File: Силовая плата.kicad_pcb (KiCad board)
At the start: 6 copper layers, 67 x 90.2 mm, 71 parts, among them J1 A, J2 B, J3 C, J4 IN-, J5 IN+, J6 Conn_02x10_Odd_Even, Q1 2N7002, Q2 2N7002, Q3 2N7002, Q4 2N7002, Q5 2N7002, Q6 2N7002, Q7 BSS214NW

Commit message: Отчётная версия
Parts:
- removed H3, H4: MountingHole, MountingHole:MountingHole_3.2mm_M3
- added J2: A, Connector_My:Power_Wire, F.Cu at (167.1, 124.9)
- added J8: A, Connector_My:Power_Wire, F.Cu at (132.2, 124.9)
- moved C1 70.7 mm to (157.0, 100.8)
- moved C10 70.7 mm to (145.6, 106.5)
- moved C12 70.7 mm to (134.1, 106.5)
- moved C14 70.7 mm to (145.6, 100.8)
- moved C16 70.7 mm to (141.7, 100.8)
- moved C17 70.7 mm to (137.9, 106.5)
- moved C18 70.7 mm to (145.6, 106.5)
- moved C19 70.7 mm to (157.0, 111.9)
- moved C2 70.7 mm to (141.7, 95.1)
- moved C21 70.7 mm to (153.2, 95.1)
- moved C22 70.7 mm to (137.9, 95.1)
- moved C24 70.7 mm to (137.9, 106.5)
- moved C25 70.7 mm to (141.7, 111.9)
- moved C26 70.7 mm to (145.6, 111.9)
- moved C27 70.7 mm to (137.9, 111.8)
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- renumbered C33 to C1, C47 to C10, C1 to C11, C6 to C12, C9 to C13, C12 to C14, C18 to C16, C21 to C17, C24 to C18, C27 to C19, C35 to C2, C40 to C20, C34 to C21, C36 to C22, C2 to C23, C7 to C24, C10 to C25, C13 to C26, C16 to C27, C19 to C28, C22 to C29, C37 to C3, C25 to C30, C28 to C31, C31 to C32, C3 to C33, C8 to C34, C11 to C35, C17 to C36, C20 to C37, C23 to C38, C26 to C39, C39 to C4, C29 to C40, C32 to C41, C38 to C43, C4 to C44, C5 to C45, C14 to C46, C30 to C47, C41 to C5, C43 to C6, C44 to C7, C45 to C8, C46 to C9, J2 to J3, J3 to J4, J4 to J5, J5 to J6, J6 to J7, Q3 to Q2, Q5 to Q3, Q2 to Q4, Q4 to Q5, R3 to R2
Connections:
- net SCL renamed SCL_MCU
- net SDA renamed SDA_MCU
- net ~{OS} renamed ~{OS}_MCU
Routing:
- net B: track 3.23 -> 12.1 mm
- net G4: track 17.6 -> 21.6 mm
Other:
- board size 67 x 90.2 mm -> 67 x 90.5 mm

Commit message: Изменил разъём 2.54мм на 2.0мм
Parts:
- J7: footprint Connector_PinSocket_2.54mm:PinSocket_2x10_P2.54mm_Vertical -> Connector_PinSocket_2.00mm:PinSocket_2x10_P2.00mm_Vertical
- moved J7 2.32 mm to (150.4, 70.7)
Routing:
- net ~{OS}_MCU: track 78.1 -> 81.5 mm
- net Shunt_1: track 14.1 -> 16.6 mm
- net G3: track 12.8 -> 14.6 mm
- net B: track 12.1 -> 13.4 mm
- net SDA_MCU: track 81.9 -> 83.0 mm
- net SCL_MCU: track 77.7 -> 78.8 mm
- net G4: track 21.6 -> 22.4 mm
- net G2: track 20.3 -> 21.1 mm
- net C: track 8.78 -> 9.44 mm

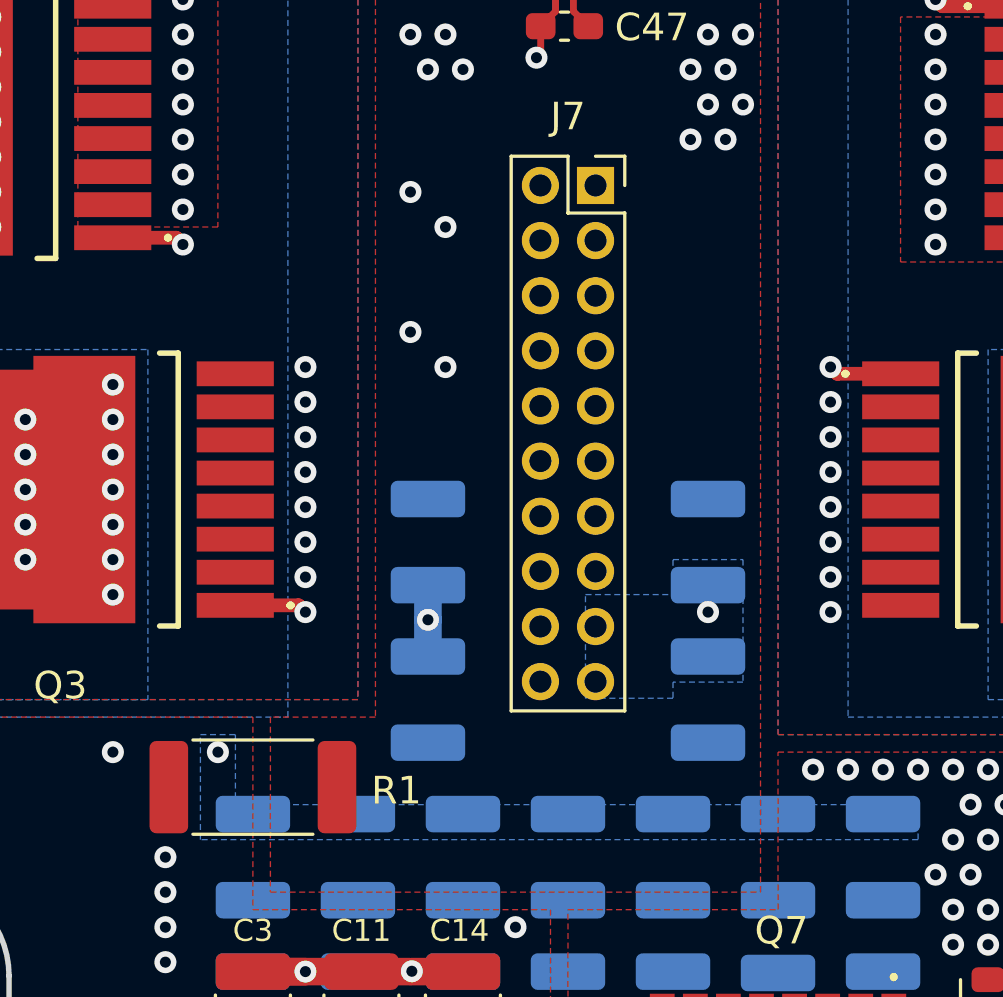
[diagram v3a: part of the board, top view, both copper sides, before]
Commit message: Убрал слабое место полигона +24В
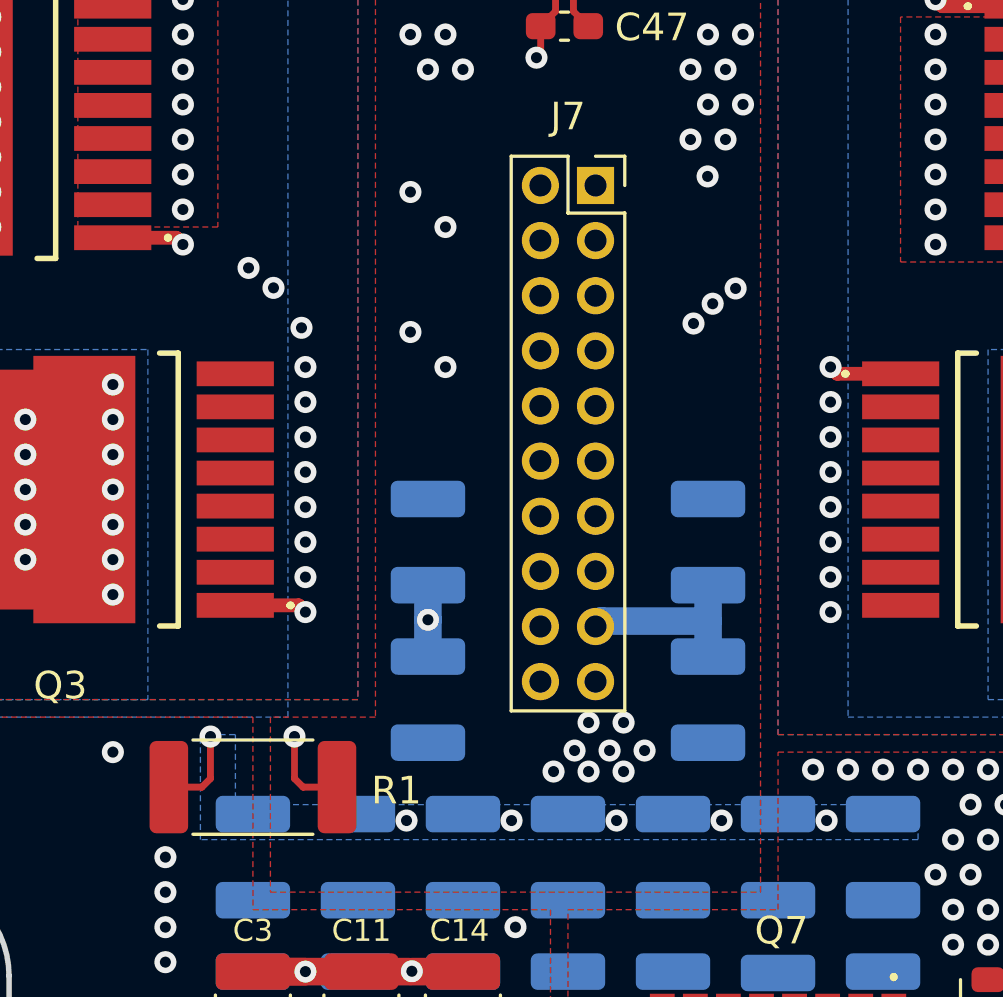
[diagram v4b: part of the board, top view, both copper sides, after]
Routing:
- net +3.3V: track 12.8 -> 100.2 mm
- net Shunt_1: track 16.6 -> 63.3 mm, vias 17 -> 21
- net Shunt_2: track 0.00 -> 12.8 mm, vias 73 -> 83
- net SDA_MCU: track 83.0 -> 84.2 mm, vias 3 -> 5
- net ~{OS}_MCU: track 81.5 -> 82.2 mm, vias 3 -> 5
- net SCL_MCU: track 78.8 -> 79.1 mm, vias 3 -> 5
- removed copper zone on In2.Cu, net +3.3V

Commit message: Первый вариант
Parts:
- removed D2, D3, D4: STLM75DS2F, Package_SO:MSOP-8_3x3mm_P0.65mm
- added C49: 10u, Capacitor_SMD:C_1206_3216Metric_Pad1.33x1.80mm_HandSolder, F.Cu at (149.6, 67.1)
- added C50: 10u, Capacitor_SMD:C_1206_3216Metric_Pad1.33x1.80mm_HandSolder, F.Cu at (144.5, 75.9)
- added C51: 10u, Capacitor_SMD:C_1206_3216Metric_Pad1.33x1.80mm_HandSolder, F.Cu at (157.2, 75.9)
- added J10: Conn_01x02_Pin, Connector_PinHeader_2.54mm:PinHeader_1x02_P2.54mm_Vertical_SMD_Pin1Left, F.Cu at (177.0, 79.2)
- added J11: Conn_01x02_Pin, Connector_PinHeader_2.54mm:PinHeader_1x02_P2.54mm_Vertical_SMD_Pin1Left, F.Cu at (163.3, 96.4)
- added J12: Conn_01x02_Pin, Connector_PinHeader_2.54mm:PinHeader_1x02_P2.54mm_Vertical_SMD_Pin1Left, F.Cu at (143.8, 84.6)
- added J13: Conn_01x02_Pin, Connector_PinHeader_2.54mm:PinHeader_1x02_P2.54mm_Vertical_SMD_Pin1Left, F.Cu at (133.6, 51.1)
- added J14: Conn_01x02_Pin, Connector_PinHeader_2.54mm:PinHeader_1x02_P2.54mm_Vertical_SMD_Pin1Left, F.Cu at (122.3, 71.9)
- added J15: Conn_01x02_Pin, Connector_PinHeader_2.54mm:PinHeader_1x02_P2.54mm_Vertical_SMD_Pin1Left, F.Cu at (122.2, 79.2)
- added J9: Conn_01x02_Pin, Connector_PinHeader_2.54mm:PinHeader_1x02_P2.54mm_Vertical_SMD_Pin1Left, F.Cu at (177.0, 71.9)
- added R3: PU2512FKGP60U5L, Resistor_SMD:R_2512_6332Metric_Pad1.40x3.35mm_HandSolder, F.Cu at (155.2, 85.6)
- C18, C30, C34, C36, C39: moved to F.Cu
- C46, C47, C48: value 0.1u -> 10u; footprint Capacitor_SMD:C_0603_1608Metric_Pad1.08x0.95mm_HandSolder -> Capacitor_SMD:C_1206_3216Metric_Pad1.33x1.80mm_HandSolder
- C5: moved to B.Cu
- J7: value Conn_02x10_Odd_Even -> Conn_01x02_Pin; footprint Connector_PinSocket_2.00mm:PinSocket_2x10_P2.00mm_Vertical -> Connector_PinHeader_2.54mm:PinHeader_1x02_P2.54mm_Vertical_SMD_Pin1Left
- moved C12 32.4 mm to (166.4, 103.4), turned to 0 degrees
- moved C48 32.1 mm to (154.7, 75.9), turned to 90 degrees
- moved C5 30.0 mm to (161.0, 92.7), turned to 180 degrees
- moved C22 28.8 mm to (166.4, 99.8), turned to 0 degrees
- moved C46 28.7 mm to (149.6, 64.5), turned to 180 degrees
- moved C24 28.4 mm to (166.4, 106.9), turned to 0 degrees
- moved C32 27.4 mm to (137.2, 92.7), turned to 0 degrees
- moved J7 25.0 mm to (165.9, 51.1), turned to 180 degrees
- moved C28 24.5 mm to (160.0, 111.3)
- moved C23 24.1 mm to (137.1, 96.3), turned to 0 degrees
- moved C36 21.4 mm to (146.3, 103.4), turned to 180 degrees
- moved C39 21.0 mm to (146.3, 96.3), turned to 180 degrees
- moved C40 20.5 mm to (152.9, 92.7), turned to 0 degrees
- moved C16 20.3 mm to (161.0, 106.9), turned to 180 degrees
- moved C38 19.9 mm to (146.3, 103.4), turned to 180 degrees
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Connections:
- C1 pad 1: Shunt_1 -> Shunt+
- C10 pad 1: Shunt_1 -> Shunt+
- C11 pad 1: Shunt_1 -> Shunt+
- C12 pad 1: Shunt_1 -> Shunt+
- C13 pad 1: Shunt_1 -> Shunt+
- C14 pad 1: Shunt_1 -> Shunt+
- C15 pad 1: Shunt_1 -> Shunt+
- C16 pad 1: Shunt_1 -> Shunt+
- C17 pad 1: Shunt_1 -> Shunt+
- C18 pad 1: Shunt_1 -> Shunt+
- C19 pad 1: Shunt_1 -> Shunt+
- C2 pad 1: Shunt_1 -> Shunt+
- C20 pad 1: Shunt_1 -> Shunt+
- C21 pad 1: Shunt_1 -> Shunt+
- C22 pad 1: Shunt_1 -> Shunt+
- C23 pad 1: Shunt_1 -> Shunt+
- C24 pad 1: Shunt_1 -> Shunt+
- C25 pad 1: Shunt_1 -> Shunt+
- C26 pad 1: Shunt_1 -> Shunt+
- C27 pad 1: Shunt_1 -> Shunt+
- C28 pad 1: Shunt_1 -> Shunt+
- C29 pad 1: Shunt_1 -> Shunt+
- C3 pad 1: Shunt_1 -> Shunt+
- C30 pad 1: Shunt_1 -> Shunt+
- C31 pad 1: Shunt_1 -> Shunt+
- C32 pad 1: Shunt_1 -> Shunt+
- C33 pad 1: Shunt_1 -> Shunt+
- C34 pad 1: Shunt_1 -> Shunt+
- C35 pad 1: Shunt_1 -> Shunt+
- C36 pad 1: Shunt_1 -> Shunt+
- C37 pad 1: Shunt_1 -> Shunt+
- C38 pad 1: Shunt_1 -> Shunt+
- C39 pad 1: Shunt_1 -> Shunt+
- C4 pad 1: Shunt_1 -> Shunt+
- C40 pad 1: Shunt_1 -> Shunt+
- C41 pad 1: Shunt_1 -> Shunt+
- C42 pad 1: Shunt_1 -> Shunt+
- C43 pad 1: Shunt_1 -> Shunt+
- C45 pad 1: Shunt_1 -> Shunt+
- C46 pad 1: +3.3V -> Shunt-
- C47 pad 1: +3.3V -> Shunt-
- C48 pad 1: +3.3V -> Shunt-
- C5 pad 1: Shunt_1 -> Shunt+
- C6 pad 1: Shunt_1 -> Shunt+
- C7 pad 1: Shunt_1 -> Shunt+
- C8 pad 1: Shunt_1 -> Shunt+
- C9 pad 1: Shunt_1 -> Shunt+
- J6 pad 1: Shunt_1 -> Shunt+
- J7 pad 1: +3.3V -> B
- J7 pad 2: ~{OS}_MCU -> G3
- Q1 pad 3: Shunt_2 -> Shunt-
- Q2 pad 3: Shunt_2 -> Shunt-
- Q3 pad 3: Shunt_2 -> Shunt-
- R1 pad 1: Shunt_1 -> Shunt+
- R1 pad 2: Shunt_2 -> Shunt-
- R2 pad 2: Shunt_1 -> Shunt+
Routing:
- net +3.3V: track 100.2 -> 0.00 mm, vias 4 -> 0
- net SDA_MCU: track 84.2 -> 0.00 mm, vias 5 -> 0
- net ~{OS}_MCU: track 82.2 -> 0.00 mm, vias 5 -> 0
- net SCL_MCU: track 79.1 -> 0.00 mm, vias 5 -> 0
- net Shunt_1: track 63.3 -> 0.00 mm, vias 21 -> 0
- net GND: track 28.5 -> 5.08 mm, vias 48 -> 118
- net Shunt-: track 0.00 -> 19.6 mm, vias 0 -> 116
- net Shunt+: track 0.00 -> 18.9 mm, vias 0 -> 67
- net B: track 13.4 -> 0.00 mm, vias 26 -> 19
- net Shunt_2: track 12.8 -> 0.00 mm, vias 83 -> 0
- net A: track 10.2 -> 0.00 mm, vias 26 -> 19
- net G3: track 14.6 -> 4.35 mm, vias 1 -> 0
- net C: track 9.44 -> 0.00 mm, vias 26 -> 19
- net G2: track 21.1 -> 28.4 mm, vias 1 -> 2
- net G5: track 11.8 -> 4.64 mm, vias 1 -> 0
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- added copper zone on In3.Cu, net A
- added copper zone on In3.Cu, net B
- added copper zone on In3.Cu, net C
- added copper zone on In3.Cu, net GND
- added copper zone on B.Cu, net Shunt+
- added copper zone on F.Cu, net Shunt+
- added copper zone on In2.Cu, net Shunt+
- added copper zone on In4.Cu, net Shunt+
- added copper zone on B.Cu, net Shunt-
- added copper zone on F.Cu, net Shunt-
- added copper zone on In2.Cu, net Shunt-
- added copper zone on In3.Cu, net Shunt-
- added copper zone on In4.Cu, net Shunt-
- removed copper zone on B.Cu, net Shunt_1
- removed copper zone on F.Cu, net Shunt_1
- removed copper zone on In3.Cu, net Shunt_1
- removed copper zone on B.Cu, net Shunt_2
- removed copper zone on F.Cu, net Shunt_2
- removed copper zone on In3.Cu, net Shunt_2

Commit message: VER2.0
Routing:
- net Shunt+: track 18.9 -> 23.0 mm, vias 67 -> 66
- net Shunt-: vias 116 -> 100
